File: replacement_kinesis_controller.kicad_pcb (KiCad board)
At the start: 2 copper layers, 99.1 x 86.4 mm, 115 parts, among them CN1 USB_general, CN2 Micro-USB, CN3 Mini-USB, CN4 USB_general, K1 CONN_3, K2 CONN_3, K3 CONN_3, K4 CONN_3, P1 CONN_3X2, P10 CONN_8, P11 CONN_5, P12 CONN_5, P13 CONN_6, P14 CONN_8, P15 CONN_5X2, P16 CONN_16, P17 CONN_16, P18 POWER, P19 PCM, P2 CONN_13, P20 UART, P21 SPI, P22 IO, P23 SMIRF, P24 CONN_2, P25 USB, P3 CONN_13, P4 CONN_10, P5 CONN_10, P6 CONN_13, P7 CONN_13, P8 CONN_5X2, P9 CONN_6, Q1 MOS_P, Q2 MOS_N, Q3 MOS_P, SW1 SW_PUSH, SW2 SW_PUSH, SW3 SPST, SW4 SPST, U1 MCP23018-E, U2 WS2811_RGB_LED, U3 WS2811_RGB_LED, U4 WS2811_RGB_LED, U5 WS2811_RGB_LED, U6 ATmega32U4, U7 WT12-A, U8 MCP73832, U9 MIC5504, X1 16MHz

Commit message: Matrix and WT12 basically done
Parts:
- moved R13 87.8 mm to (115.9, 91.8), turned to 180 degrees
- moved Q2 87.0 mm to (115.9, 88.6), turned to 90 degrees
- moved R15 86.3 mm to (115.9, 85.4), turned to 0 degrees
- moved Q3 85.9 mm to (115.9, 82.2), turned to 90 degrees
- moved R17 85.8 mm to (115.9, 76.5), turned to 180 degrees
- moved R16 85.8 mm to (115.9, 79.1), turned to 0 degrees
- moved R11 55.5 mm to (97.8, 105.4)
- moved C17 55.5 mm to (95.2, 105.4)
- moved C18 55.5 mm to (109.2, 105.4)
- moved C20 55.5 mm to (111.8, 105.4)
- moved D17 55.5 mm to (102.9, 105.4)
- moved Q1 55.5 mm to (106.0, 105.4)
- moved U9 55.5 mm to (114.9, 105.4)
- moved C19 55.5 mm to (92.7, 105.4)
- moved R14 55.5 mm to (100.3, 105.4)
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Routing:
- net PB4: track 27.7 -> 158.2 mm, vias 0 -> 4
- net COL_5: track 20.9 -> 117.7 mm, vias 0 -> 4
- net ROW_L7: track 67.7 -> 163.1 mm, vias 1 -> 3
- net COL_4: track 21.9 -> 102.1 mm, vias 0 -> 4
- net PB6: track 28.6 -> 104.9 mm, vias 0 -> 3
- net PF0: track 20.9 -> 89.0 mm
- net ROW_L5: track 53.8 -> 117.8 mm, vias 0 -> 2
- net PB3: track 42.8 -> 104.0 mm
- net ROW_L2: track 41.3 -> 99.3 mm, vias 2 -> 4
- net PB1: track 40.8 -> 93.8 mm, vias 2 -> 4
- net ROW_L0: track 12.5 -> 64.6 mm
- net PF1: track 57.0 -> 97.7 mm
- net PD3: track 6.03 -> 44.0 mm, vias 0 -> 1
- net PF5: track 62.6 -> 99.4 mm
- net W_USB_D+: track 0.00 -> 35.3 mm, vias 0 -> 2
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
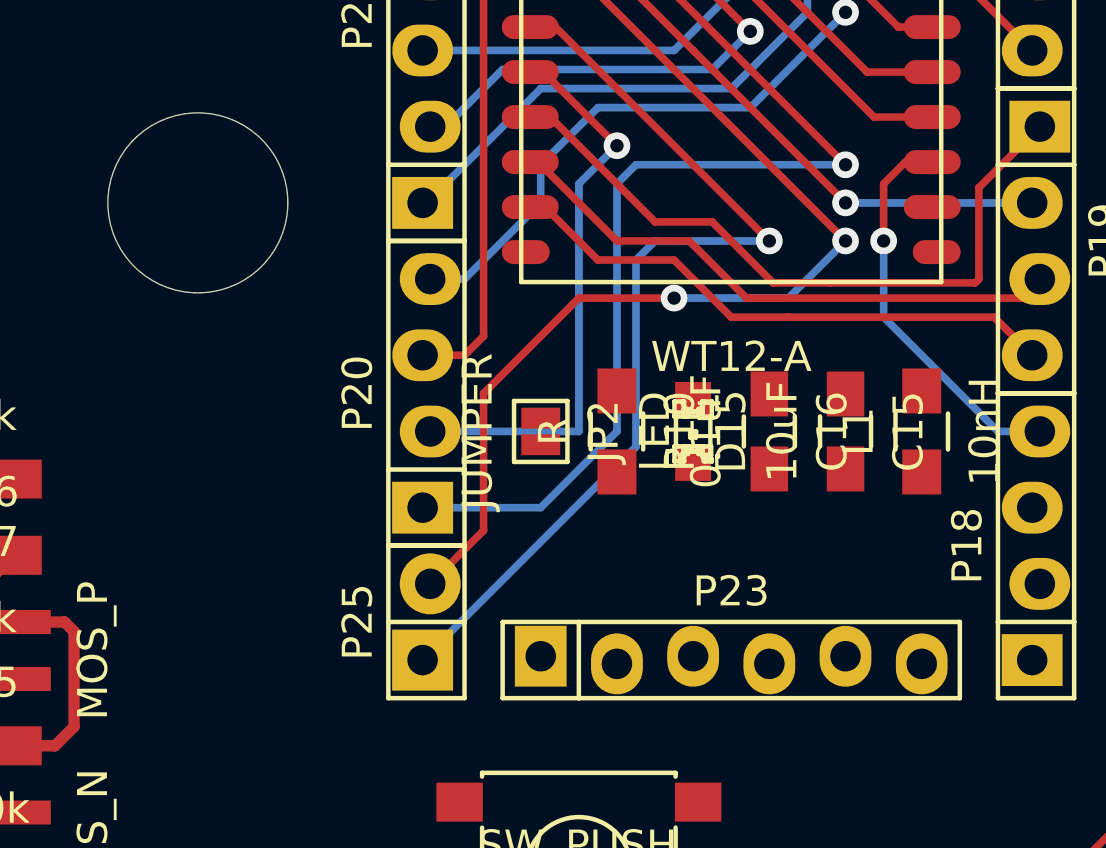
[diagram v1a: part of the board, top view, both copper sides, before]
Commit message: More WT12 wiring
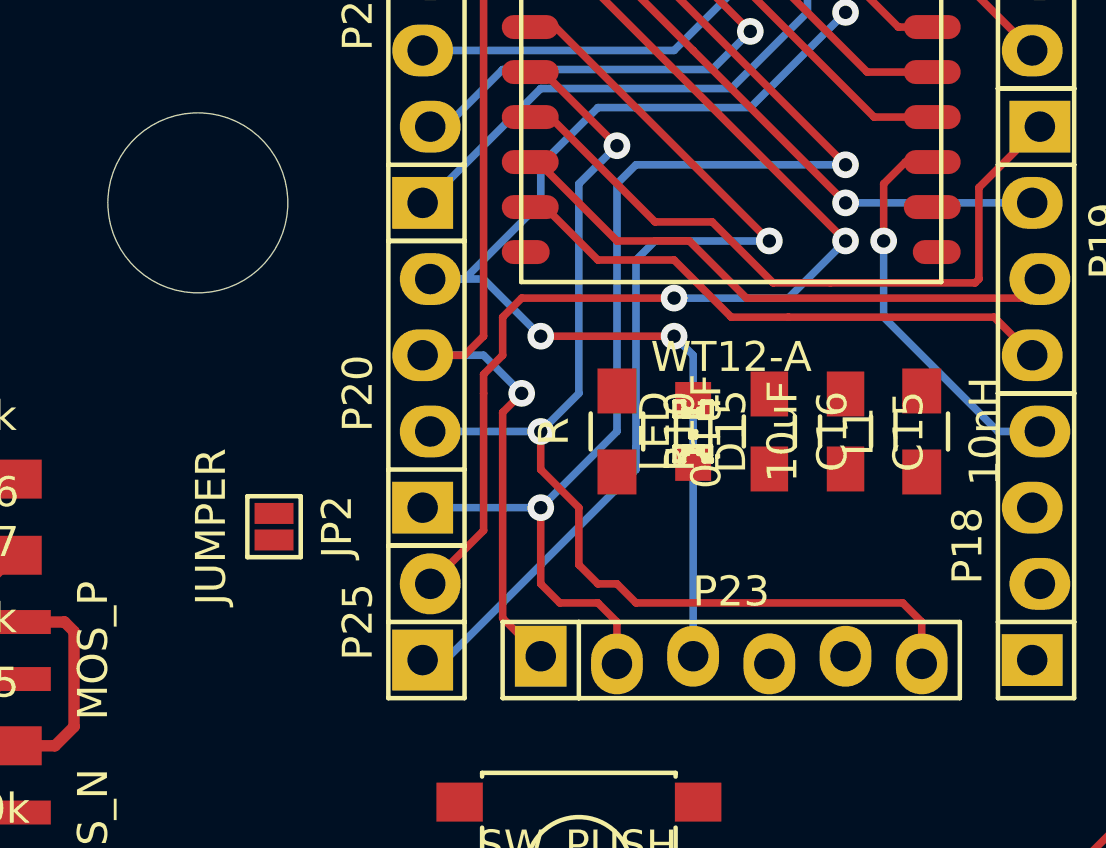
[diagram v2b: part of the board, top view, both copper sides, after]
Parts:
- moved JP2 9.44 mm to (125.7, 78.1)
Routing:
- net PD2: track 34.7 -> 54.5 mm, vias 1 -> 3
- net W_NCTS: track 18.9 -> 36.8 mm, vias 1 -> 2
- net W_NRTS: track 19.9 -> 33.3 mm, vias 0 -> 1
- net PD3: track 44.0 -> 51.0 mm, vias 1 -> 2
- net W_USB_D+: track 35.3 -> 36.5 mm

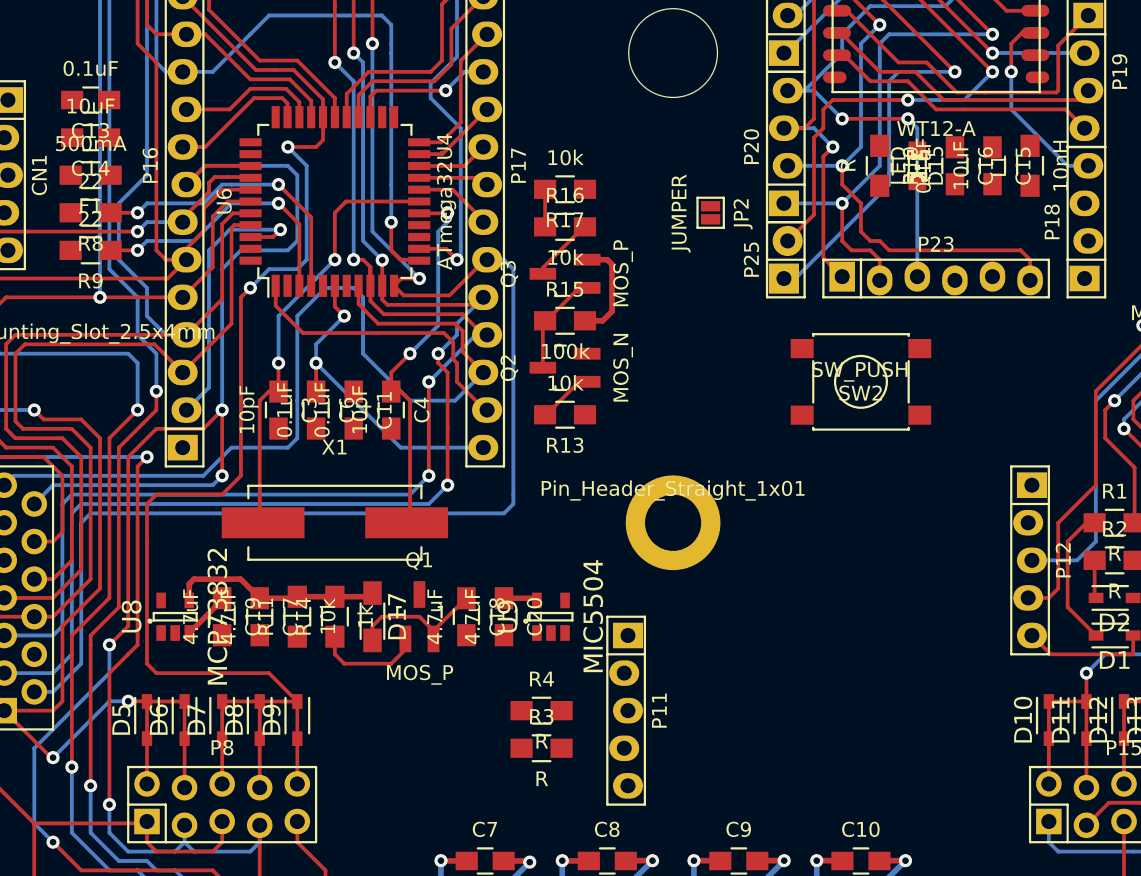
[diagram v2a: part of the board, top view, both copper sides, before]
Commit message: Initial run of I2C lines
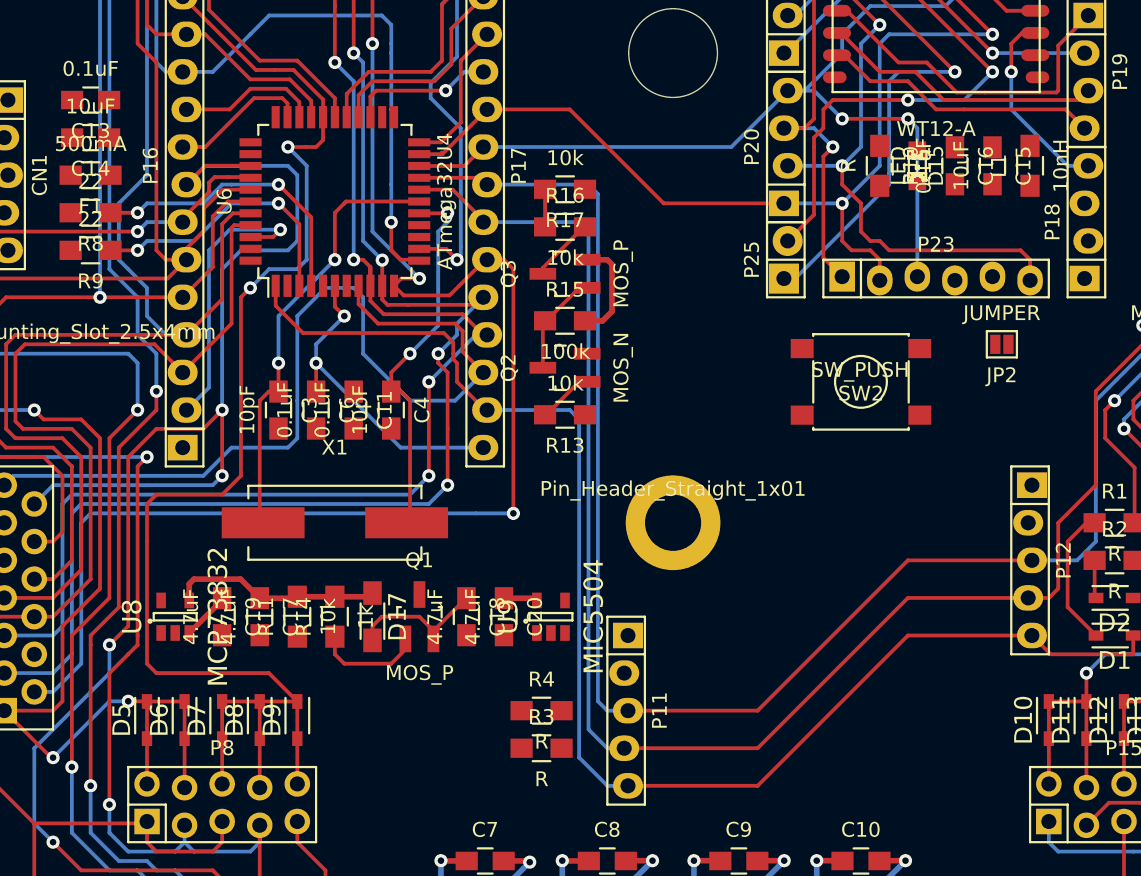
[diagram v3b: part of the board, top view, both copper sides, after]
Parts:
- moved JP2 21.6 mm to (145.4, 87.0), turned to 180 degrees
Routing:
- net PD1: track 33.6 -> 109.5 mm
- net PD0: track 37.4 -> 112.8 mm
- net PE6: track 28.6 -> 93.5 mm
- net PD3: track 51.0 -> 73.7 mm
- net PD2: track 54.5 -> 76.7 mm
- net PB3: track 104.0 -> 104.3 mm, vias 3 -> 4

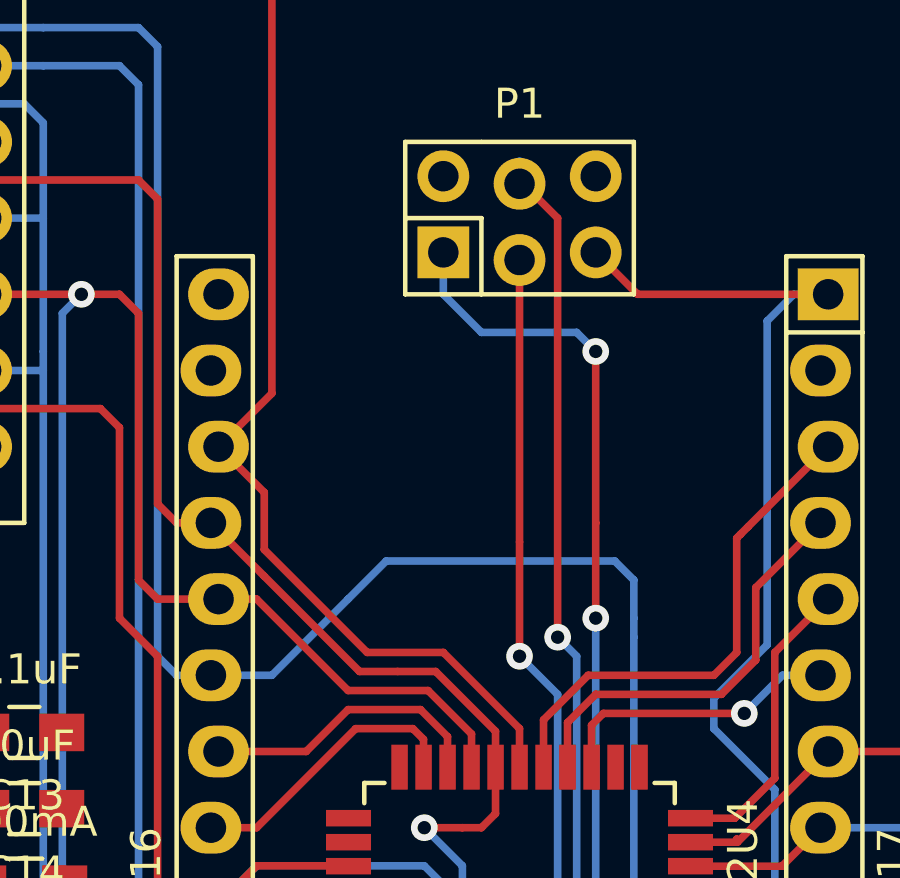
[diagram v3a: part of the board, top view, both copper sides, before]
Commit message: Rearranged some traces
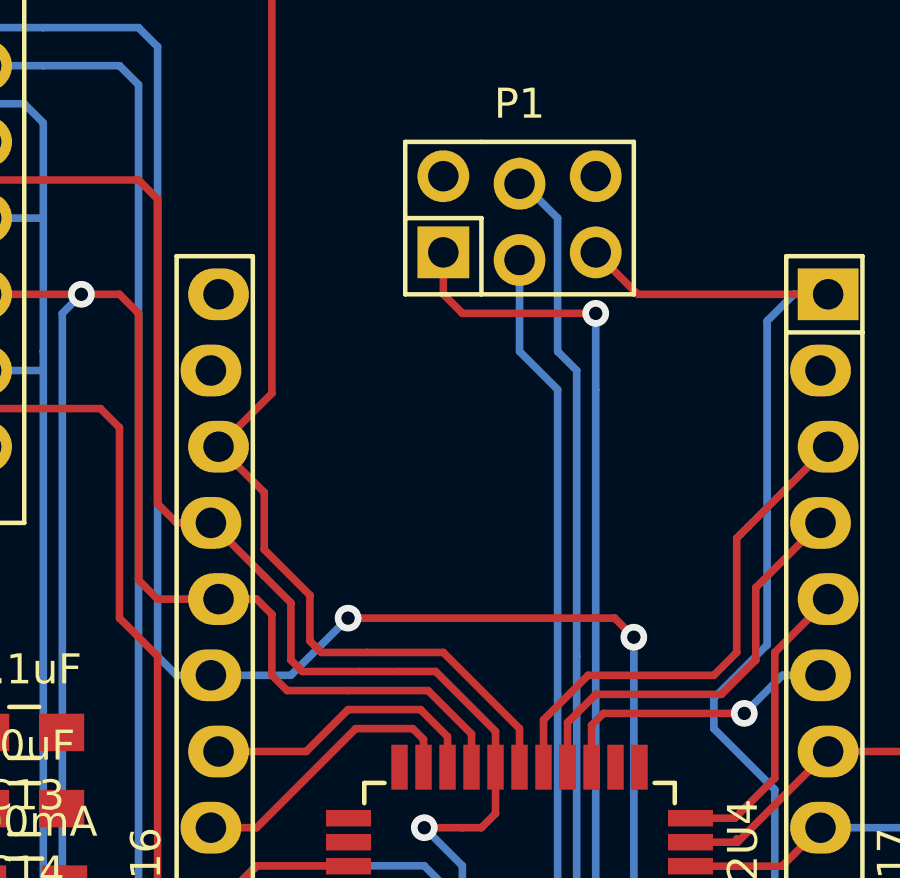
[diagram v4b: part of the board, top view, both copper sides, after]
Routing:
- net ROW_L7: track 163.1 -> 160.4 mm, vias 3 -> 5
- net PB6: track 104.9 -> 106.1 mm
- net ROW_L5: track 117.8 -> 119.0 mm
- net PB4: track 158.2 -> 159.1 mm
- net PB3: track 104.3 -> 105.1 mm, vias 4 -> 3
- net ROW_L2: track 99.3 -> 99.5 mm, vias 4 -> 3
- net PB1: vias 4 -> 3

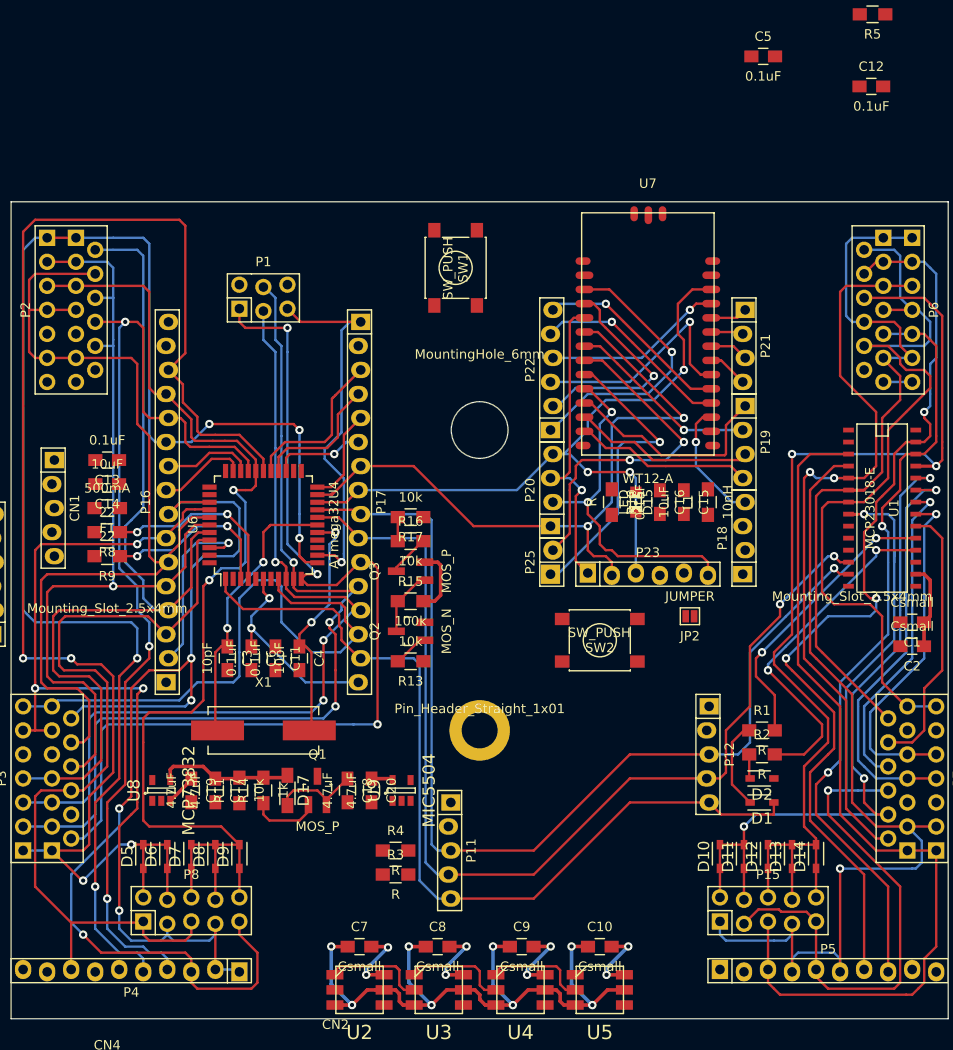
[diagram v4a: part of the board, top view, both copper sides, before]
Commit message: Shoehorned another cap into the 32u4 breakout area
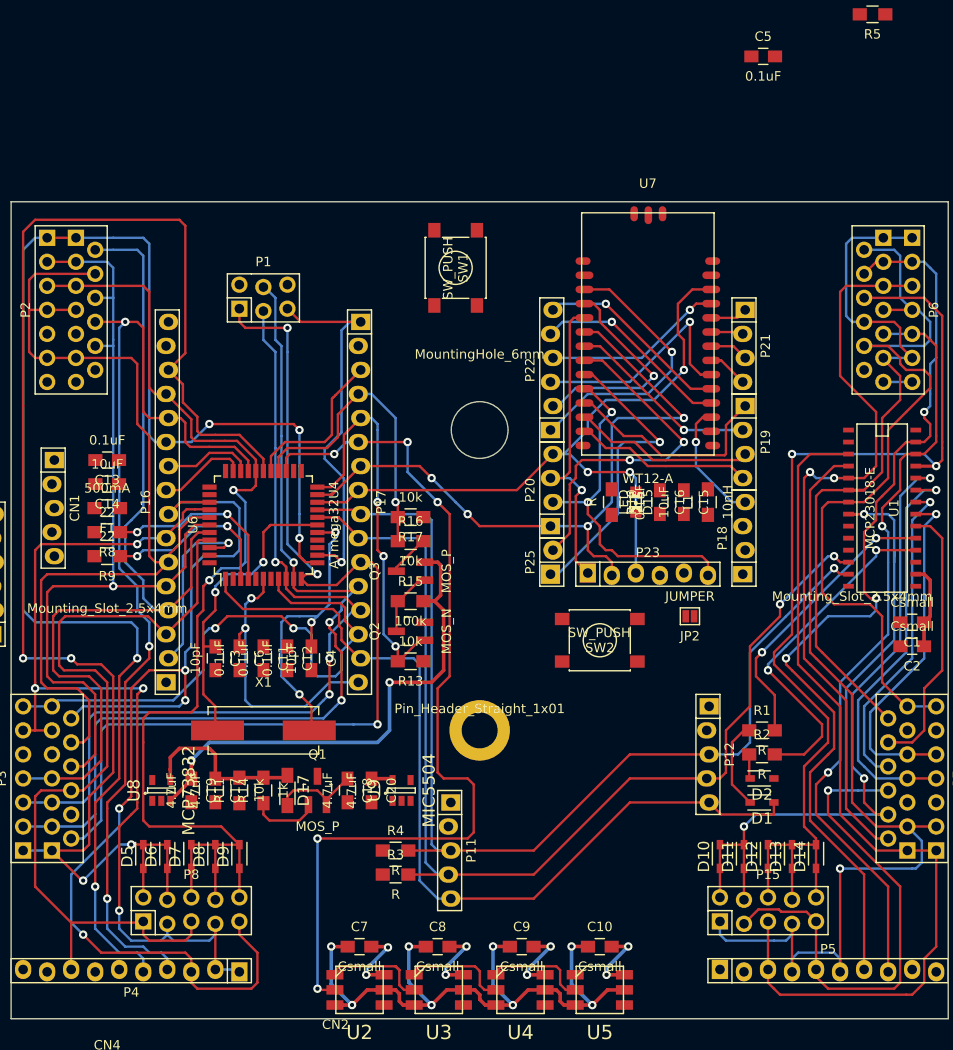
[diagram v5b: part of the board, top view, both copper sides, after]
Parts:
- moved C12 86.4 mm to (102.9, 91.4), turned to 270 degrees
- moved C11 1.27 mm to (100.3, 91.4)
- moved C3 1.27 mm to (95.2, 91.4)
- moved C4 1.27 mm to (105.4, 91.4)
- moved C6 1.27 mm to (97.8, 91.4)
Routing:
- net LED_DATA: track 9.72 -> 96.2 mm, vias 1 -> 5
- net +BATT: track 10.3 -> 54.7 mm, vias 0 -> 2
- net PD5: track 13.8 -> 41.9 mm, vias 0 -> 3
- net PD6: track 16.6 -> 32.2 mm, vias 0 -> 1
- net +3.3V: track 21.9 -> 29.4 mm
- net Net-(C4-Pad1): track 25.5 -> 32.0 mm, vias 2 -> 3
- net PD1: track 109.5 -> 114.0 mm
- net PD0: track 112.8 -> 117.1 mm
- net +5V: track 14.3 -> 18.1 mm
- net Net-(C3-Pad1): track 29.6 -> 33.0 mm
- net ROW_L0: track 64.6 -> 62.2 mm, vias 0 -> 2
- net COL_5: track 117.7 -> 116.2 mm
- net ROW_L2: track 99.5 -> 100.0 mm
- net PD3: vias 2 -> 4

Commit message: Add power switch connectors
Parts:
- moved D16 95.1 mm to (52.1, 121.3)
- moved R12 95.1 mm to (52.1, 118.1)
- moved SW4 56.4 mm to (108.6, 117.5), turned to 270 degrees
- moved SW3 56.2 mm to (108.6, 111.1), turned to 270 degrees
- moved R18 55.0 mm to (101.6, 117.5), turned to 270 degrees
- moved JP3 53.0 mm to (102.9, 113.0), turned to 0 degrees
- moved R19 51.5 mm to (104.1, 117.5), turned to 270 degrees
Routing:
- net Net-(JP3-Pad1): track 0.00 -> 29.6 mm, vias 0 -> 2
- net Net-(SW4-Pad2): track 0.00 -> 18.6 mm
- net Net-(Q1-PadD): track 0.00 -> 14.8 mm, vias 0 -> 1
- net Net-(C18-Pad1): track 9.98 -> 21.1 mm
- net +BATT: track 54.7 -> 64.4 mm
- net Net-(JP3-Pad3): track 0.00 -> 3.25 mm
